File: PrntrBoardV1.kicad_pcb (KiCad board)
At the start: 4 copper layers, 99 x 99 mm, 225 parts, among them J1 EXT 5V, J10 Probe, J11 Extruder Heater, J12 Stepper, J13 Thermistor, J14 Max, J15 Min, J16 Max, J17 Min, J18 Max, J19 Min, J2 Bed Heater, J20 Stepper, J21 Stepper, J22 Stepper, J23 Stepper, J24 Probe, J25 Extruder Heater, J26 Stepper, J27 Thermistor, J28 Thermistor, J29 12-24V, J3 Z Probe, J30 LCD, J4 E0 Cool, J5 E0 Part, J6 E1 Cool, J7 E1 Part, J8 Always On Fan 1, J9 Always On Fan 2, U1 4078, U11 NUCLEO-64, U2 74HCT02, U3 74LVC125, U4 TMC5130, U5 TMC5130, U6 TMC5130, U7 TMC5130, U8 TMC5130, X1 16MHz

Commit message: Update FID* to SMD from virtual component, so they show up in the pick-and-place output.
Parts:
- C10, C11, C12, C13, C24, C25, C26, C27, C37, C38, C39, C40, C50, C51, C52, C53, C63, C64, C65, C66: value 1000pF >50V -> 1000pF
- D10, D11, D2: value HEATER -> LED
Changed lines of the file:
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@@
-(kicad_pcb (version 20171130) (host pcbnew 5.0.0-rc2-unknown-6090f90~65~ubuntu18.04.1)
+(kicad_pcb (version 20171130) (host pcbnew 5.0.0-rc2-unknown-7b73557~65~ubuntu18.04.1)
   (general
     (thickness 1.6)
@@
   )
   (setup
-    (last_trace_width 0.3)
+    (last_trace_width 0.1524)
     (user_trace_width 0.1524)
     (user_trace_width 0.2032)
@@
       (hpglpennumber 1)
       (hpglpenspeed 20)
-      (hpglpendiameter 15)
+      (hpglpendiameter 15.000000)
       (psnegative false)
       (psa4output false)
@@
       (effects (font (size 1 1) (thickness 0.15)))
     )
-    (fp_text value HEATER (at 0 1.45 90) (layer F.Fab)
+    (fp_text value LED (at 0 1.45 90) (layer F.Fab)
       (effects (font (size 1 1) (thickness 0.15)))
     )
@@
       (effects (font (size 1 1) (thickness 0.15)))
     )
-    (fp_text value HEATER (at 0 1.45 90) (layer F.Fab)
+    (fp_text value LED (at 0 1.45 90) (layer F.Fab)
       (effects (font (size 1 1) (thickness 0.15)))
     )
@@
       (effects (font (size 1 1) (thickness 0.15)))
     )
-    (fp_text value HEATER (at 0 1.45 90) (layer F.Fab)
+    (fp_text value LED (at 0 1.45 90) (layer F.Fab)
       (effects (font (size 1 1) (thickness 0.15)))
     )
@@
       (effects (font (size 1 1) (thickness 0.15)))
     )
-    (fp_text value "1000pF >50V" (at 0 1.45 270) (layer F.Fab)
+    (fp_text value 1000pF (at 0 1.45 270) (layer F.Fab)
       (effects (font (size 1 1) (thickness 0.15)))
     )
@@
       (effects (font (size 1 1) (thickness 0.15)))
     )
-    (fp_text value "1000pF >50V" (at 0 1.45 180) (layer F.Fab)
+    (fp_text value 1000pF (at 0 1.45 180) (layer F.Fab)
       (effects (font (size 1 1) (thickness 0.15)))
     )
@@
       (effects (font (size 1 1) (thickness 0.15)))
     )
-    (fp_text value "1000pF >50V" (at 0 1.45 90) (layer F.Fab)
+    (fp_text value 1000pF (at 0 1.45 90) (layer F.Fab)
       (effects (font (size 1 1) (thickness 0.15)))
     )
@@
       (effects (font (size 1 1) (thickness 0.15)))
     )
-    (fp_text value "1000pF >50V" (at 0 1.45) (layer F.Fab)
+    (fp_text value 1000pF (at 0 1.45) (layer F.Fab)
       (effects (font (size 1 1) (thickness 0.15)))
     )
@@
       (effects (font (size 1 1) (thickness 0.15)))
     )
-    (fp_text value "1000pF >50V" (at 0 1.45 90) (layer F.Fab)
+    (fp_text value 1000pF (at 0 1.45 90) (layer F.Fab)
       (effects (font (size 1 1) (thickness 0.15)))
     )
@@
       (effects (font (size 1 1) (thickness 0.15)))
     )
-    (fp_text value "1000pF >50V" (at 0 1.45 180) (layer F.Fab)
+    (fp_text value 1000pF (at 0 1.45 180) (layer F.Fab)
       (effects (font (size 1 1) (thickness 0.15)))
     )
@@
       (effects (font (size 1 1) (thickness 0.15)))
     )
-    (fp_text value "1000pF >50V" (at 0 1.45 270) (layer F.Fab)
+    (fp_text value 1000pF (at 0 1.45 270) (layer F.Fab)
       (effects (font (size 1 1) (thickness 0.15)))
     )
@@
       (effects (font (size 1 1) (thickness 0.15)))
     )
-    (fp_text value "1000pF >50V" (at 0 1.45) (layer F.Fab)
+    (fp_text value 1000pF (at 0 1.45) (layer F.Fab)
       (effects (font (size 1 1) (thickness 0.15)))
     )
@@
       (effects (font (size 1 1) (thickness 0.15)))
     )
-    (fp_text value "1000pF >50V" (at 0 1.45 270) (layer F.Fab)
+    (fp_text value 1000pF (at 0 1.45 270) (layer F.Fab)
       (effects (font (size 1 1) (thickness 0.15)))
     )
@@
       (effects (font (size 1 1) (thickness 0.15)))
     )
-    (fp_text value "1000pF >50V" (at 0 1.45) (layer F.Fab)
+    (fp_text value 1000pF (at 0 1.45) (layer F.Fab)
       (effects (font (size 1 1) (thickness 0.15)))
     )
@@
       (effects (font (size 1 1) (thickness 0.15)))
     )
-    (fp_text value "1000pF >50V" (at 0 1.45) (layer F.Fab)
+    (fp_text value 1000pF (at 0 1.45) (layer F.Fab)
       (effects (font (size 1 1) (thickness 0.15)))
     )
@@
       (effects (font (size 1 1) (thickness 0.15)))
     )
-    (fp_text value "1000pF >50V" (at 0 1.45 90) (layer F.Fab)
+    (fp_text value 1000pF (at 0 1.45 90) (layer F.Fab)
       (effects (font (size 1 1) (thickness 0.15)))
     )
@@
       (effects (font (size 1 1) (thickness 0.15)))
     )
-    (fp_text value "1000pF >50V" (at 0 1.45 270) (layer F.Fab)
+    (fp_text value 1000pF (at 0 1.45 270) (layer F.Fab)
       (effects (font (size 1 1) (thickness 0.15)))
     )
@@
       (effects (font (size 1 1) (thickness 0.15)))
     )
-    (fp_text value "1000pF >50V" (at 0 1.45 90) (layer F.Fab)
+    (fp_text value 1000pF (at 0 1.45 90) (layer F.Fab)
       (effects (font (size 1 1) (thickness 0.15)))
     )
@@
       (effects (font (size 1 1) (thickness 0.15)))
     )
-    (fp_text value "1000pF >50V" (at 0 1.45 270) (layer F.Fab)
+    (fp_text value 1000pF (at 0 1.45 270) (layer F.Fab)
       (effects (font (size 1 1) (thickness 0.15)))
     )
@@
       (effects (font (size 1 1) (thickness 0.15)))
     )
-    (fp_text value "1000pF >50V" (at 0 1.45) (layer F.Fab)
+    (fp_text value 1000pF (at 0 1.45) (layer F.Fab)
       (effects (font (size 1 1) (thickness 0.15)))
     )
@@
       (effects (font (size 1 1) (thickness 0.15)))
     )
-    (fp_text value "1000pF >50V" (at 0 1.45 180) (layer F.Fab)
+    (fp_text value 1000pF (at 0 1.45 180) (layer F.Fab)
       (effects (font (size 1 1) (thickness 0.15)))
     )
@@
       (effects (font (size 1 1) (thickness 0.15)))
     )
-    (fp_text value "1000pF >50V" (at 0 1.45 180) (layer F.Fab)
+    (fp_text value 1000pF (at 0 1.45 180) (layer F.Fab)
       (effects (font (size 1 1) (thickness 0.15)))
     )
@@
       (effects (font (size 1 1) (thickness 0.15)))
     )
-    (fp_text value "1000pF >50V" (at 0 1.45 90) (layer F.Fab)
+    (fp_text value 1000pF (at 0 1.45 90) (layer F.Fab)
       (effects (font (size 1 1) (thickness 0.15)))
     )
@@
       (effects (font (size 1 1) (thickness 0.15)))
     )
-    (fp_text value "1000pF >50V" (at 0 1.45) (layer F.Fab)
+    (fp_text value 1000pF (at 0 1.45) (layer F.Fab)
       (effects (font (size 1 1) (thickness 0.15)))
     )
@@
     (descr "Circular Fiducial, 1mm bare copper top; 2.54mm keepout")
     (tags marker)
-    (attr virtual)
+    (attr smd)
     (fp_text reference FID1 (at 0 2.9845) (layer F.SilkS)
       (effects (font (size 1 1) (thickness 0.15)))
@@
     (descr "Circular Fiducial, 1mm bare copper top; 2.54mm keepout")
     (tags marker)
-    (attr virtual)
+    (attr smd)
     (fp_text reference FID4 (at 0 -2.7305) (layer F.SilkS)
       (effects (font (size 1 1) (thickness 0.15)))
@@
     (descr "Circular Fiducial, 1mm bare copper top; 2.54mm keepout")
     (tags marker)
-    (attr virtual)
+    (attr smd)
     (fp_text reference FID3 (at -0.0508 -2.4892) (layer F.SilkS)
       (effects (font (size 1 1) (thickness 0.15)))
@@
     (descr "Circular Fiducial, 1mm bare copper top; 2.54mm keepout")
     (tags marker)
-    (attr virtual)
+    (attr smd)
     (fp_text reference FID2 (at 0.1344 3.3292) (layer F.SilkS)
       (effects (font (size 1 1) (thickness 0.15)))

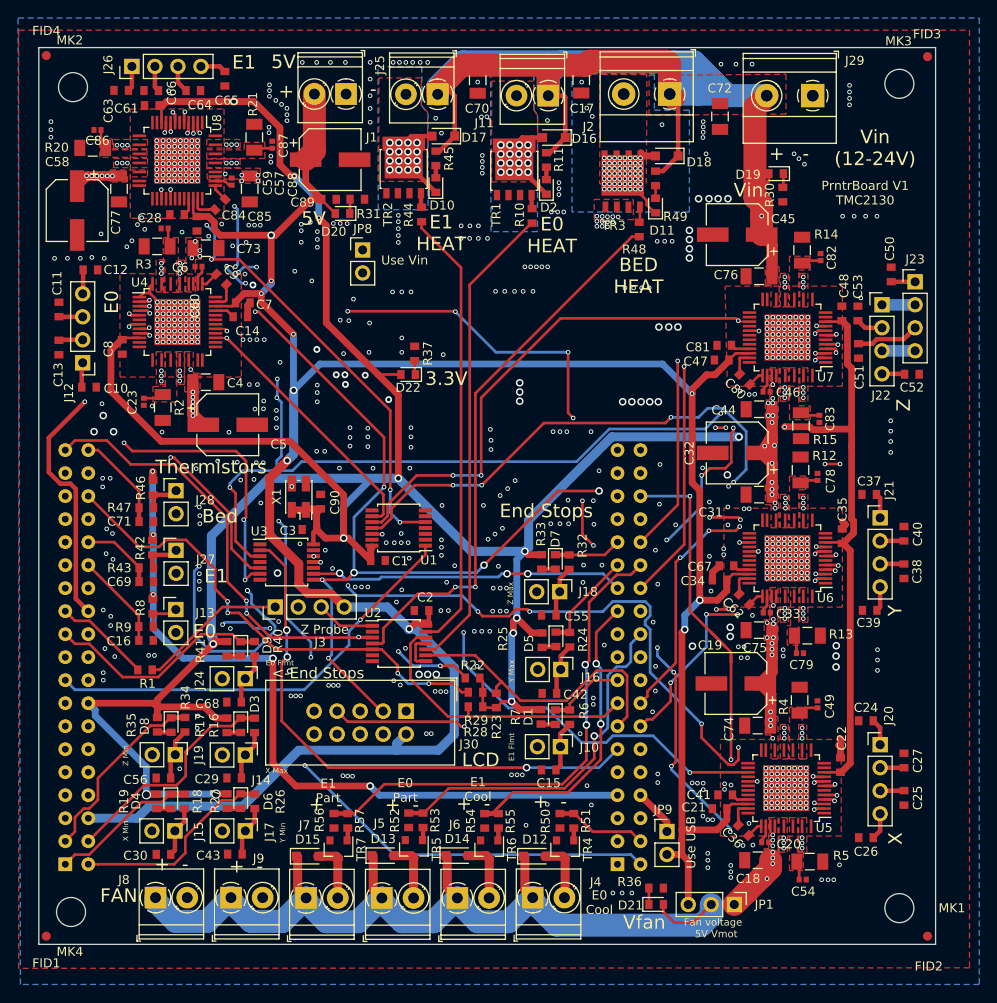
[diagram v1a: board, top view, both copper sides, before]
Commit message: Cherry pick path names changes.
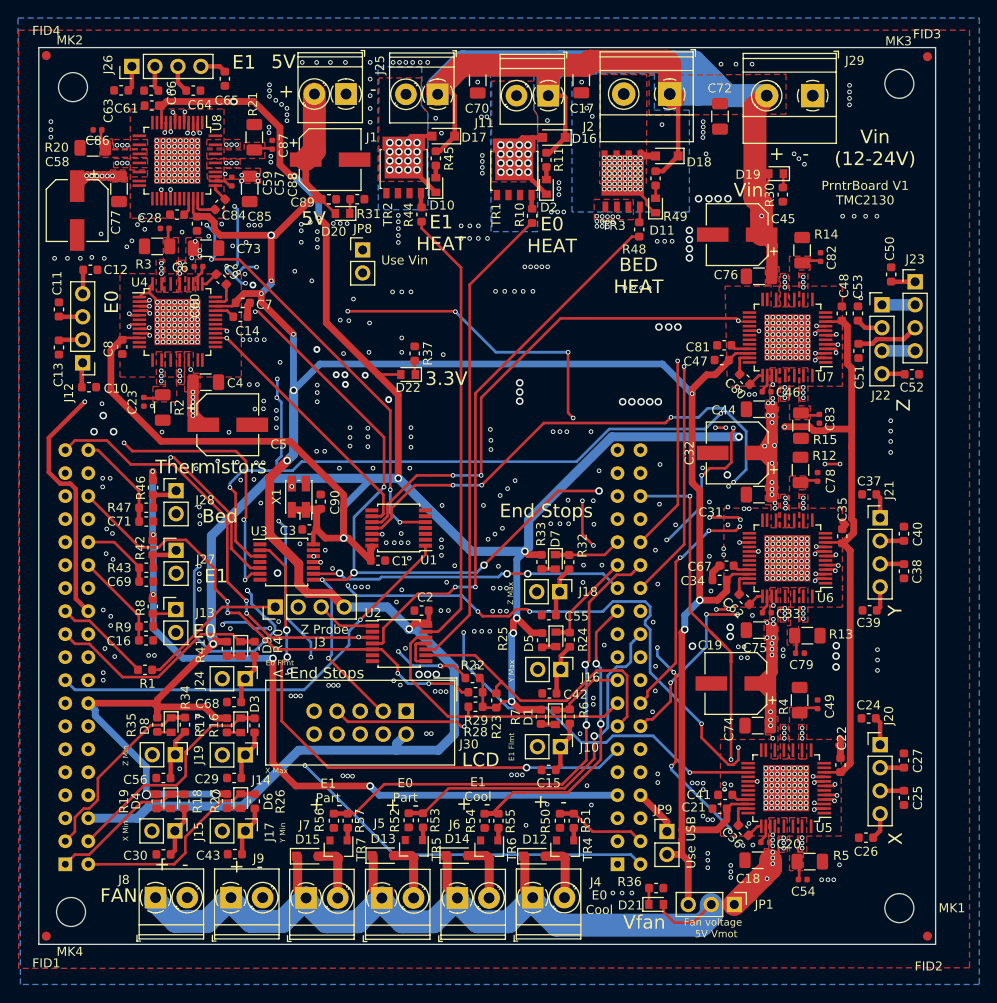
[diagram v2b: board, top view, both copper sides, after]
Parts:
- moved C24 0.40 mm to (111.6, 93.0)
- moved R6 0.09 mm to (78.6, 92.8)
